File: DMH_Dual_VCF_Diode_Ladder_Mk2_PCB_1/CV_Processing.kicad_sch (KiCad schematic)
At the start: 58 parts, among them J15 Conn_01x08_PinHeader, J16 Conn_01x08_PinHeader, SW10 SW_DPDT_OnOn, SW7 SW_SPDT_OnOffOn, SW9 SW_SPDT_OnOffOn, U7 TL074, U8 TL074

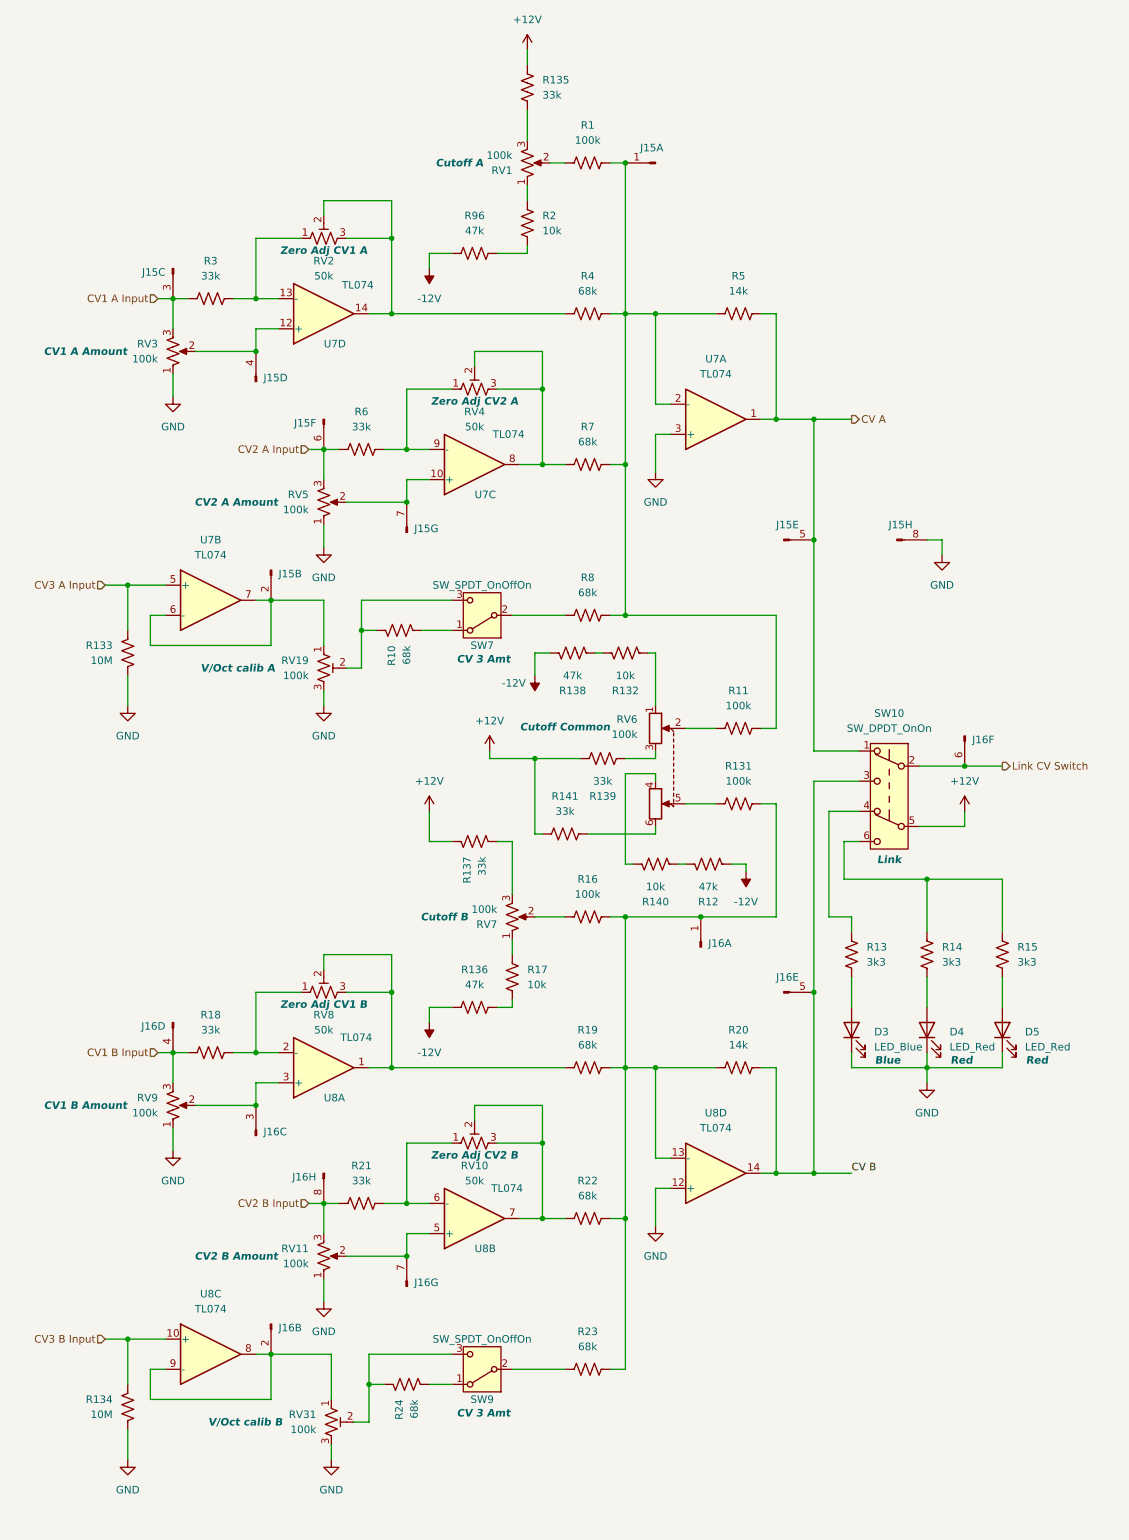
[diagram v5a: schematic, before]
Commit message: Synchronized changes from PCB 1 to PCB 2 schematic
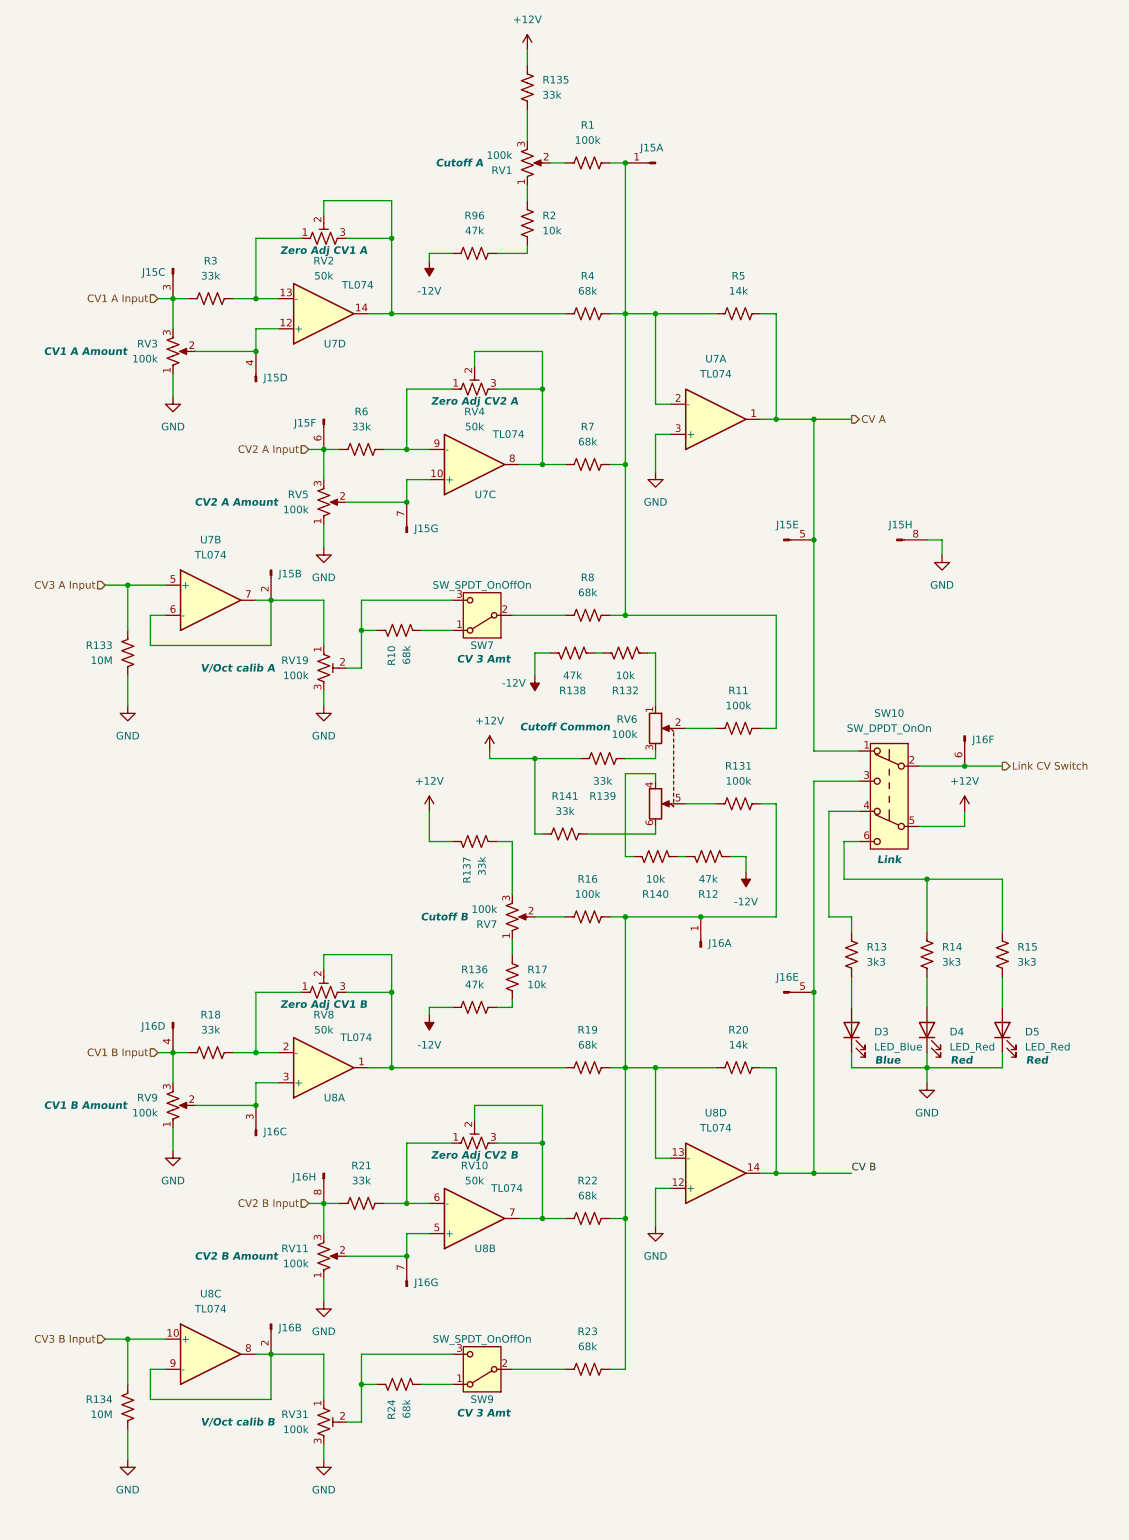
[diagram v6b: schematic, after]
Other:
- moved on the sheet: R12, R140, R24, RV31
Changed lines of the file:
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@@
 	)
 	(junction
-		(at 71.12 243.84)
+		(at 69.85 243.84)
 		(diameter 0)
 		(color 0 0 0 0)
@@
 	(wire
 		(pts
-			(xy 81.28 180.34) (xy 81.28 182.88)
+			(xy 81.28 180.34) (xy 81.28 181.61)
 		)
 		(stroke
@@
 	(wire
 		(pts
-			(xy 81.28 243.84) (xy 85.09 243.84)
+			(xy 80.01 243.84) (xy 85.09 243.84)
 		)
 		(stroke
@@
 	(wire
 		(pts
-			(xy 81.28 53.34) (xy 81.28 55.88)
+			(xy 81.28 53.34) (xy 81.28 54.61)
 		)
 		(stroke
@@
 	(wire
 		(pts
-			(xy 85.09 238.76) (xy 71.12 238.76)
+			(xy 85.09 238.76) (xy 69.85 238.76)
 		)
 		(stroke
@@
 	(wire
 		(pts
-			(xy 134.62 156.21) (xy 134.62 157.48)
+			(xy 134.62 154.94) (xy 134.62 157.48)
 		)
 		(stroke
@@
 	(wire
 		(pts
-			(xy 64.77 238.76) (xy 54.61 238.76)
+			(xy 63.5 238.76) (xy 54.61 238.76)
 		)
 		(stroke
@@
 	(wire
 		(pts
-			(xy 132.08 156.21) (xy 134.62 156.21)
+			(xy 132.08 154.94) (xy 134.62 154.94)
 		)
 		(stroke
@@
 	(wire
 		(pts
-			(xy 71.12 243.84) (xy 73.66 243.84)
-		)
-		(stroke
-			(width 0)
-			(type default)
-		)
-	)
-	(wire
-		(pts
 			(xy 101.6 38.1) (xy 104.14 38.1)
 		)
@@
 	(wire
 		(pts
-			(xy 114.3 156.21) (xy 115.57 156.21)
+			(xy 114.3 154.94) (xy 115.57 154.94)
 		)
 		(stroke
@@
 	(wire
 		(pts
-			(xy 64.77 254) (xy 64.77 256.54)
+			(xy 63.5 254) (xy 63.5 256.54)
 		)
 		(stroke
@@
 	(wire
 		(pts
-			(xy 123.19 156.21) (xy 124.46 156.21)
+			(xy 123.19 154.94) (xy 124.46 154.94)
 		)
 		(stroke
@@
 	(wire
 		(pts
-			(xy 71.12 250.19) (xy 71.12 243.84)
+			(xy 69.85 250.19) (xy 69.85 243.84)
 		)
 		(stroke
@@
 	(wire
 		(pts
-			(xy 71.12 238.76) (xy 71.12 243.84)
+			(xy 69.85 238.76) (xy 69.85 243.84)
 		)
 		(stroke
@@
 	(wire
 		(pts
-			(xy 114.3 140.97) (xy 114.3 156.21)
+			(xy 114.3 140.97) (xy 114.3 154.94)
 		)
 		(stroke
@@
 	(wire
 		(pts
+			(xy 69.85 243.84) (xy 72.39 243.84)
+		)
+		(stroke
+			(width 0)
+			(type default)
+		)
+	)
+	(wire
+		(pts
 			(xy 114.3 190.5) (xy 114.3 215.9)
 		)
@@
 	(wire
 		(pts
-			(xy 64.77 246.38) (xy 64.77 238.76)
+			(xy 63.5 246.38) (xy 63.5 238.76)
 		)
 		(stroke
@@
 	(wire
 		(pts
-			(xy 68.58 250.19) (xy 71.12 250.19)
+			(xy 67.31 250.19) (xy 69.85 250.19)
 		)
 		(stroke
@@
 	(symbol
 		(lib_id "Device:R_Potentiometer_Trim_US")
-		(at 64.77 250.19 0)
+		(at 63.5 250.19 0)
 		(unit 1)
 		(exclude_from_sim no)
@@
 		(dnp no)
 		(property "Reference" "RV31"
-			(at 62.23 248.9199 0)
+			(at 60.96 248.9199 0)
 			(effects
 				(font
@@
 		)
 		(property "Value" "100k"
-			(at 62.23 251.4599 0)
+			(at 60.96 251.4599 0)
 			(effects
 				(font
@@
 		)
 		(property "Footprint" ""
-			(at 64.77 250.19 0)
+			(at 63.5 250.19 0)
 			(effects
 				(font
@@
 		)
 		(property "Datasheet" "~"
-			(at 64.77 250.19 0)
+			(at 63.5 250.19 0)
 			(effects
 				(font
@@
 		)
 		(property "Description" "Trim-potentiometer, US symbol"
-			(at 64.77 250.19 0)
+			(at 63.5 250.19 0)
 			(effects
 				(font
@@
 		)
 		(property "Function" "V/Oct calib B"
-			(at 50.292 250.19 0)
+			(at 49.022 250.19 0)
 			(effects
 				(font
@@
 	(symbol
 		(lib_id "power:GND")
-		(at 64.77 256.54 0)
+		(at 63.5 256.54 0)
 		(unit 1)
 		(exclude_from_sim no)
@@
 		(fields_autoplaced yes)
 		(property "Reference" "#PWR030"
-			(at 64.77 262.89 0)
+			(at 63.5 262.89 0)
 			(effects
 				(font
@@
 		)
 		(property "Value" "GND"
-			(at 64.77 261.62 0)
+			(at 63.5 261.62 0)
 			(effects
 				(font
@@
 		)
 		(property "Footprint" ""
-			(at 64.77 256.54 0)
+			(at 63.5 256.54 0)
 			(effects
 				(font
@@
 		)
 		(property "Datasheet" ""
-			(at 64.77 256.54 0)
+			(at 63.5 256.54 0)
 			(effects
 				(font
@@
 		)
 		(property "Description" "Power symbol creates a global label with name \"GND\" , ground"
-			(at 64.77 256.54 0)
+			(at 63.5 256.54 0)
 			(effects
 				(font
@@
 	(symbol
 		(lib_id "Device:R_US")
-		(at 119.38 156.21 270)
+		(at 119.38 154.94 270)
 		(mirror x)
 		(unit 1)
@@
 		(dnp no)
 		(property "Reference" "R140"
-			(at 119.38 162.56 90)
+			(at 119.38 161.29 90)
 			(effects
 				(font
@@
 		)
 		(property "Value" "10k"
-			(at 119.38 160.02 90)
+			(at 119.38 158.75 90)
 			(effects
 				(font
@@
 		)
 		(property "Footprint" "Resistor_THT:R_Axial_DIN0207_L6.3mm_D2.5mm_P7.62mm_Horizontal"
-			(at 119.126 155.194 90)
+			(at 119.126 153.924 90)
 			(effects
 				(font
@@
 		)
 		(property "Datasheet" "~"
-			(at 119.38 156.21 0)
+			(at 119.38 154.94 0)
 			(effects
 				(font
@@
 		)
 		(property "Description" "Resistor, US symbol"
-			(at 119.38 156.21 0)
+			(at 119.38 154.94 0)
 			(effects
 				(font
@@
 	(symbol
 		(lib_id "Device:R_US")
-		(at 77.47 243.84 270)
+		(at 76.2 243.84 270)
 		(mirror x)
 		(unit 1)
@@
 		(dnp no)
 		(property "Reference" "R24"
-			(at 76.1999 246.38 0)
+			(at 74.9299 246.38 0)
 			(effects
 				(font
@@
 		)
 		(property "Value" "68k"
-			(at 78.7399 246.38 0)
+			(at 77.4699 246.38 0)
 			(effects
 				(font
@@
 		)
 		(property "Footprint" "Resistor_THT:R_Axial_DIN0207_L6.3mm_D2.5mm_P7.62mm_Horizontal"
-			(at 77.216 242.824 90)
+			(at 75.946 242.824 90)
 			(effects
 				(font
@@
 		)
 		(property "Datasheet" "~"
-			(at 77.47 243.84 0)
+			(at 76.2 243.84 0)
 			(effects
 				(font
@@
 		)
 		(property "Description" "Resistor, US symbol"
-			(at 77.47 243.84 0)
+			(at 76.2 243.84 0)
 			(effects
 				(font
@@
 		)
 		(property "Function" ""
-			(at 77.47 243.84 0)
+			(at 76.2 243.84 0)
 			(effects
 				(font
@@
 	(symbol
 		(lib_id "Device:R_US")
-		(at 128.27 156.21 270)
+		(at 128.27 154.94 270)
 		(mirror x)
 		(unit 1)
@@
 		(dnp no)
 		(property "Reference" "R12"
-			(at 128.27 162.56 90)
+			(at 128.27 161.29 90)
 			(effects
 				(font
@@
 		)
 		(property "Value" "47k"
-			(at 128.27 160.02 90)
+			(at 128.27 158.75 90)
 			(effects
 				(font
@@
 		)
 		(property "Footprint" "Resistor_THT:R_Axial_DIN0207_L6.3mm_D2.5mm_P7.62mm_Horizontal"
-			(at 128.016 155.194 90)
+			(at 128.016 153.924 90)
 			(effects
 				(font
@@
 		)
 		(property "Datasheet" "~"
-			(at 128.27 156.21 0)
+			(at 128.27 154.94 0)
 			(effects
 				(font
@@
 		)
 		(property "Description" "Resistor, US symbol"
-			(at 128.27 156.21 0)
+			(at 128.27 154.94 0)
 			(effects
 				(font
@@
 	(symbol
 		(lib_id "power:-12V")
-		(at 81.28 55.88 180)
+		(at 81.28 54.61 180)
 		(unit 1)
 		(exclude_from_sim no)
@@
 		(fields_autoplaced yes)
 		(property "Reference" "#PWR010"
-			(at 81.28 52.07 0)
+			(at 81.28 50.8 0)
 			(effects
 				(font
@@
 		)
 		(property "Value" "-12V"
-			(at 81.28 60.96 0)
+			(at 81.28 59.69 0)
 			(effects
 				(font
@@
 		)
 		(property "Footprint" ""
-			(at 81.28 55.88 0)
+			(at 81.28 54.61 0)
 			(effects
 				(font
@@
 		)
 		(property "Datasheet" ""
-			(at 81.28 55.88 0)
+			(at 81.28 54.61 0)
 			(effects
 				(font
@@
 		)
 		(property "Description" "Power symbol creates a global label with name \"-12V\""
-			(at 81.28 55.88 0)
+			(at 81.28 54.61 0)
 			(effects
 				(font
@@
 	(symbol
 		(lib_id "power:-12V")
-		(at 81.28 182.88 180)
+		(at 81.28 181.61 180)
 		(unit 1)
 		(exclude_from_sim no)
@@
 		(fields_autoplaced yes)
 		(property "Reference" "#PWR025"
-			(at 81.28 179.07 0)
+			(at 81.28 177.8 0)
 			(effects
 				(font
@@
 		)
 		(property "Value" "-12V"
-			(at 81.28 187.96 0)
+			(at 81.28 186.69 0)
 			(effects
 				(font
@@
 		)
 		(property "Footprint" ""
-			(at 81.28 182.88 0)
+			(at 81.28 181.61 0)
 			(effects
 				(font
@@
 		)
 		(property "Datasheet" ""
-			(at 81.28 182.88 0)
+			(at 81.28 181.61 0)
 			(effects
 				(font
@@
 		)
 		(property "Description" "Power symbol creates a global label with name \"-12V\""
-			(at 81.28 182.88 0)
+			(at 81.28 181.61 0)
 			(effects
 				(font

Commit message: Finished Mk2.0
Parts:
- U7, U8: footprint (none) -> Package_DIP:DIP-14_W7.62mm_Socket
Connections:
- net at R24.2, RV31.2: now also SW9.1 (A); no longer SW9.3 (C)
- net at SW7.1 (A): now also R10.2, RV19.2; no longer R10.1
- net at R24.1: now also SW9.3 (C); no longer SW9.1 (A)
- new net: R10.1, SW7.3 (C)
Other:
- moved on the sheet: SW7, SW9
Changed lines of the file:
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@@
 			)
 		)
-		(property "Footprint" ""
+		(property "Footprint" "Package_DIP:DIP-14_W7.62mm_Socket"
 			(at 43.18 236.22 0)
 			(effects
@@
 	(symbol
 		(lib_id "Switch:SW_SPDT")
-		(at 90.17 114.3 180)
+		(at 90.17 114.3 0)
+		(mirror y)
 		(unit 1)
 		(exclude_from_sim no)
@@
 		(dnp no)
 		(property "Reference" "SW7"
-			(at 90.17 119.38 0)
+			(at 90.17 109.22 0)
 			(effects
 				(font
@@
 		)
 		(property "Value" "SW_SPDT_OnOffOn"
-			(at 90.17 109.22 0)
+			(at 90.17 119.38 0)
 			(effects
 				(font
@@
 		)
 		(property "Datasheet" "~"
-			(at 90.17 106.68 0)
+			(at 90.17 121.92 0)
 			(effects
 				(font
@@
 		)
 		(property "Function" "CV 3 Amt"
-			(at 90.424 121.666 0)
+			(at 90.424 106.934 0)
 			(effects
 				(font
@@
 	(symbol
 		(lib_id "Switch:SW_SPDT")
-		(at 90.17 241.3 180)
+		(at 90.17 241.3 0)
+		(mirror y)
 		(unit 1)
 		(exclude_from_sim no)
@@
 		(dnp no)
 		(property "Reference" "SW9"
-			(at 90.17 246.38 0)
+			(at 90.17 236.22 0)
 			(effects
 				(font
@@
 		)
 		(property "Value" "SW_SPDT_OnOffOn"
-			(at 90.17 236.22 0)
+			(at 90.17 246.38 0)
 			(effects
 				(font
@@
 		)
 		(property "Datasheet" "~"
-			(at 90.17 233.68 0)
+			(at 90.17 248.92 0)
 			(effects
 				(font
@@
 		)
 		(property "Function" "CV 3 Amt"
-			(at 90.424 248.666 0)
+			(at 90.424 233.934 0)
 			(effects
 				(font
@@
 			)
 		)
-		(property "Footprint" ""
+		(property "Footprint" "Package_DIP:DIP-14_W7.62mm_Socket"
 			(at 43.18 109.22 0)
 			(effects

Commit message: Exported BoM
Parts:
- RV19, RV31: footprint (none) -> Potentiometer_THT:Potentiometer_Bourns_3296W_Vertical
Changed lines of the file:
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@@
 			)
 		)
-		(property "Footprint" ""
+		(property "Footprint" "Potentiometer_THT:Potentiometer_Bourns_3296W_Vertical"
 			(at 63.5 250.19 0)
 			(effects
@@
 			)
 		)
-		(property "Footprint" ""
+		(property "Footprint" "Potentiometer_THT:Potentiometer_Bourns_3296W_Vertical"
 			(at 63.5 123.19 0)
 			(effects
